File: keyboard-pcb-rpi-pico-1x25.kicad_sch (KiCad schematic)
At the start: 28 parts, among them SW1 SW_Push, SW10 SW_Push, SW11 SW_Push, SW12 SW_Push, SW13 SW_Push, SW14 SW_Push, SW15 SW_Push, SW16 SW_Push, SW17 SW_Push, SW18 SW_Push, SW19 SW_Push, SW2 SW_Push, SW20 SW_Push, SW21 SW_Push, SW22 SW_Push, SW23 SW_Push, SW24 SW_Push, SW25 SW_Push, SW3 SW_Push, SW4 SW_Push, SW5 SW_Push, SW6 SW_Push, SW7 SW_Push, SW8 SW_Push, SW9 SW_Push

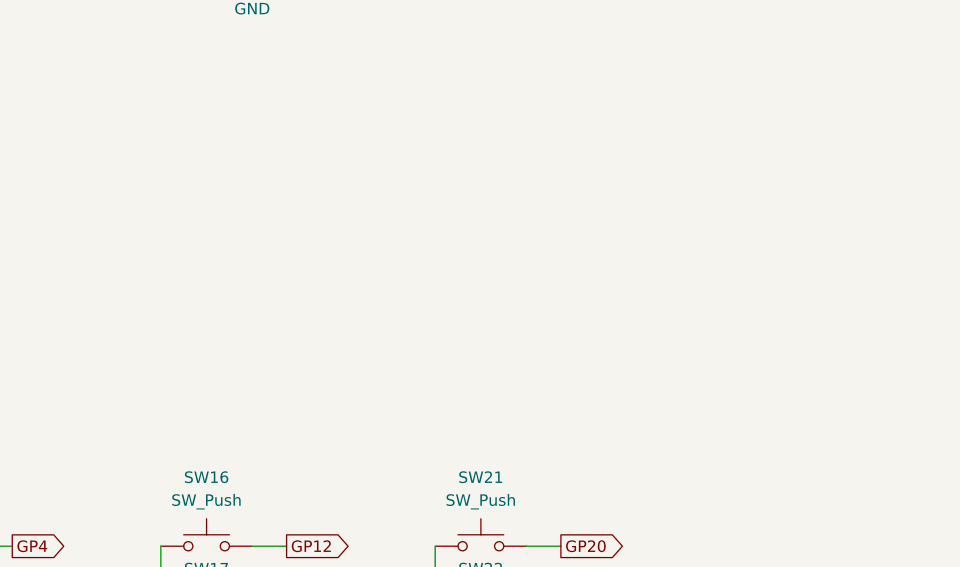
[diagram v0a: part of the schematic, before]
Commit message: Add mounting holes and art
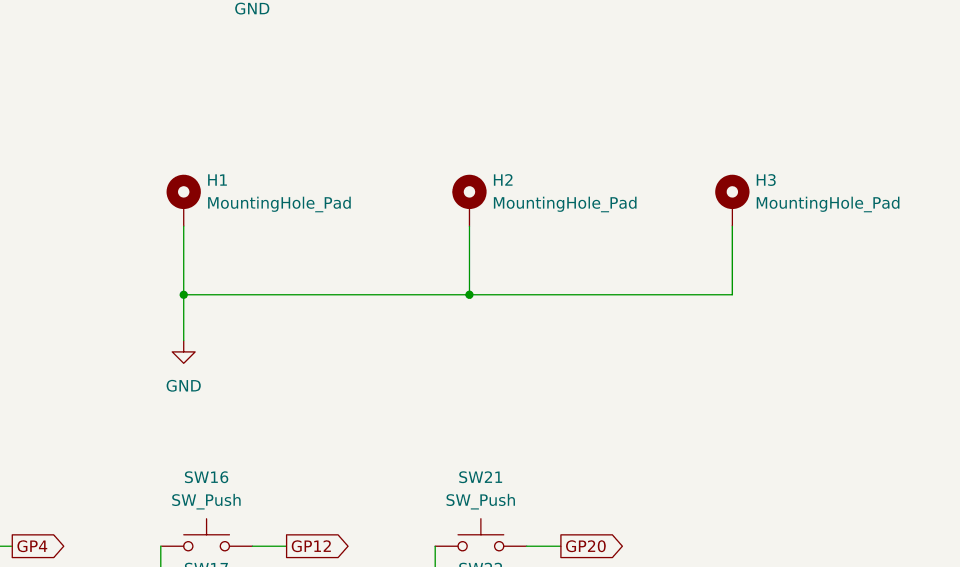
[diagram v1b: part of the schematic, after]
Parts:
- added H1, H2, H3: MountingHole_Pad, MountingHole:MountingHole_3.2mm_M3_Pad, symbol Mechanical:MountingHole_Pad
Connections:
- net GND: now also H1.1, H2.1, H3.1

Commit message: Fix width of Pico pin headers
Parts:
- SW1, SW10, SW11, SW12, SW13, SW14, SW15, SW16, SW17, SW18, SW19, SW2, SW20, SW21, SW22, SW23, SW24, SW25, SW3, SW4, SW5, SW6, SW7, SW8, SW9: footprint library:SW_Cherry_MX_1.00u_PCB -> Button_Switch_Keyboard:SW_Cherry_MX_1.00u_PCB
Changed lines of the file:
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@@
 			)
 		)
-		(property "Footprint" "library:SW_Cherry_MX_1.00u_PCB"
+		(property "Footprint" "Button_Switch_Keyboard:SW_Cherry_MX_1.00u_PCB"
 			(at 66.04 116.84 0)
 			(effects
@@
 			)
 		)
-		(property "Footprint" "library:SW_Cherry_MX_1.00u_PCB"
+		(property "Footprint" "Button_Switch_Keyboard:SW_Cherry_MX_1.00u_PCB"
 			(at 157.48 106.68 0)
 			(effects
@@
 			)
 		)
-		(property "Footprint" "library:SW_Cherry_MX_1.00u_PCB"
+		(property "Footprint" "Button_Switch_Keyboard:SW_Cherry_MX_1.00u_PCB"
 			(at 96.52 96.52 0)
 			(effects
@@
 			)
 		)
-		(property "Footprint" "library:SW_Cherry_MX_1.00u_PCB"
+		(property "Footprint" "Button_Switch_Keyboard:SW_Cherry_MX_1.00u_PCB"
 			(at 35.56 106.68 0)
 			(effects
@@
 			)
 		)
-		(property "Footprint" "library:SW_Cherry_MX_1.00u_PCB"
+		(property "Footprint" "Button_Switch_Keyboard:SW_Cherry_MX_1.00u_PCB"
 			(at 66.04 96.52 0)
 			(effects
@@
 			)
 		)
-		(property "Footprint" "library:SW_Cherry_MX_1.00u_PCB"
+		(property "Footprint" "Button_Switch_Keyboard:SW_Cherry_MX_1.00u_PCB"
 			(at 96.52 127 0)
 			(effects
@@
 			)
 		)
-		(property "Footprint" "library:SW_Cherry_MX_1.00u_PCB"
+		(property "Footprint" "Button_Switch_Keyboard:SW_Cherry_MX_1.00u_PCB"
 			(at 96.52 106.68 0)
 			(effects
@@
 			)
 		)
-		(property "Footprint" "library:SW_Cherry_MX_1.00u_PCB"
+		(property "Footprint" "Button_Switch_Keyboard:SW_Cherry_MX_1.00u_PCB"
 			(at 127 137.16 0)
 			(effects
@@
 			)
 		)
-		(property "Footprint" "library:SW_Cherry_MX_1.00u_PCB"
+		(property "Footprint" "Button_Switch_Keyboard:SW_Cherry_MX_1.00u_PCB"
 			(at 35.56 116.84 0)
 			(effects
@@
 			)
 		)
-		(property "Footprint" "library:SW_Cherry_MX_1.00u_PCB"
+		(property "Footprint" "Button_Switch_Keyboard:SW_Cherry_MX_1.00u_PCB"
 			(at 66.04 137.16 0)
 			(effects
@@
 			)
 		)
-		(property "Footprint" "library:SW_Cherry_MX_1.00u_PCB"
+		(property "Footprint" "Button_Switch_Keyboard:SW_Cherry_MX_1.00u_PCB"
 			(at 35.56 127 0)
 			(effects
@@
 			)
 		)
-		(property "Footprint" "library:SW_Cherry_MX_1.00u_PCB"
+		(property "Footprint" "Button_Switch_Keyboard:SW_Cherry_MX_1.00u_PCB"
 			(at 66.04 106.68 0)
 			(effects
@@
 			)
 		)
-		(property "Footprint" "library:SW_Cherry_MX_1.00u_PCB"
+		(property "Footprint" "Button_Switch_Keyboard:SW_Cherry_MX_1.00u_PCB"
 			(at 96.52 137.16 0)
 			(effects
@@
 			)
 		)
-		(property "Footprint" "library:SW_Cherry_MX_1.00u_PCB"
+		(property "Footprint" "Button_Switch_Keyboard:SW_Cherry_MX_1.00u_PCB"
 			(at 157.48 127 0)
 			(effects
@@
 			)
 		)
-		(property "Footprint" "library:SW_Cherry_MX_1.00u_PCB"
+		(property "Footprint" "Button_Switch_Keyboard:SW_Cherry_MX_1.00u_PCB"
 			(at 35.56 137.16 0)
 			(effects
@@
 			)
 		)
-		(property "Footprint" "library:SW_Cherry_MX_1.00u_PCB"
+		(property "Footprint" "Button_Switch_Keyboard:SW_Cherry_MX_1.00u_PCB"
 			(at 157.48 116.84 0)
 			(effects
@@
 			)
 		)
-		(property "Footprint" "library:SW_Cherry_MX_1.00u_PCB"
+		(property "Footprint" "Button_Switch_Keyboard:SW_Cherry_MX_1.00u_PCB"
 			(at 66.04 127 0)
 			(effects
@@
 			)
 		)
-		(property "Footprint" "library:SW_Cherry_MX_1.00u_PCB"
+		(property "Footprint" "Button_Switch_Keyboard:SW_Cherry_MX_1.00u_PCB"
 			(at 35.56 96.52 0)
 			(effects
@@
 			)
 		)
-		(property "Footprint" "library:SW_Cherry_MX_1.00u_PCB"
+		(property "Footprint" "Button_Switch_Keyboard:SW_Cherry_MX_1.00u_PCB"
 			(at 127 116.84 0)
 			(effects
@@
 			)
 		)
-		(property "Footprint" "library:SW_Cherry_MX_1.00u_PCB"
+		(property "Footprint" "Button_Switch_Keyboard:SW_Cherry_MX_1.00u_PCB"
 			(at 157.48 137.16 0)
 			(effects
@@
 			)
 		)
-		(property "Footprint" "library:SW_Cherry_MX_1.00u_PCB"
+		(property "Footprint" "Button_Switch_Keyboard:SW_Cherry_MX_1.00u_PCB"
 			(at 127 96.52 0)
 			(effects
@@
 			)
 		)
-		(property "Footprint" "library:SW_Cherry_MX_1.00u_PCB"
+		(property "Footprint" "Button_Switch_Keyboard:SW_Cherry_MX_1.00u_PCB"
 			(at 127 106.68 0)
 			(effects
@@
 			)
 		)
-		(property "Footprint" "library:SW_Cherry_MX_1.00u_PCB"
+		(property "Footprint" "Button_Switch_Keyboard:SW_Cherry_MX_1.00u_PCB"
 			(at 157.48 96.52 0)
 			(effects
@@
 			)
 		)
-		(property "Footprint" "library:SW_Cherry_MX_1.00u_PCB"
+		(property "Footprint" "Button_Switch_Keyboard:SW_Cherry_MX_1.00u_PCB"
 			(at 96.52 116.84 0)
 			(effects
@@
 			)
 		)
-		(property "Footprint" "library:SW_Cherry_MX_1.00u_PCB"
+		(property "Footprint" "Button_Switch_Keyboard:SW_Cherry_MX_1.00u_PCB"
 			(at 127 127 0)
 			(effects
